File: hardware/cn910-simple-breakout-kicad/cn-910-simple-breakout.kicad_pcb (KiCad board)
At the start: 2 copper layers, 35 x 35 mm, 8 parts, among them J1 CN910_FPC_CON, J2 J_PB_RF, J3 J_REC_RF

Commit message: Enhanced CN910 breakout KiCad project with updated design rules, added new components, and refined PCB layout. Introduced a new simple breakout PCB with detailed Gerber files for manufacturing. Updated project metadata and library references for improved organization.
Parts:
- added R1: 470, Resistor_SMD:R_0603_1608Metric, F.Cu at (167.8, 93.3)
- added R2: 470, Resistor_SMD:R_0603_1608Metric, F.Cu at (167.8, 103.1)
- added TP2: TP_PB_RF, TestPoint:TestPoint_Pad_1.5x1.5mm, F.Cu at (168.4, 90.2)
- added TP3: TP_REC_RF, TestPoint:TestPoint_Pad_1.5x1.5mm, F.Cu at (172.7, 102.5)
- added TP4: TP_LANC_SIG, TestPoint:TestPoint_Loop_D2.50mm_Drill1.0mm, F.Cu at (151.1, 82.9)
- added TP5: TP_XCPC_IN, TestPoint:TestPoint_Loop_D2.50mm_Drill1.0mm, F.Cu at (155.2, 87.5)
- added TP6: TP_GND, TestPoint:TestPoint_Loop_D2.50mm_Drill1.0mm, F.Cu at (171.3, 96.4)
- moved TP1 9.24 mm to (160.5, 82.1)
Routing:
- net /LANC_SIG: track 0.00 -> 9.97 mm
- net /XCPC_IN: track 0.00 -> 9.58 mm
- net /REC_RF: track 19.9 -> 25.0 mm
- net /PB_RF: track 14.6 -> 19.4 mm
- net Net-(R2-Pad2): track 0.00 -> 4.47 mm
- net GND: vias 65 -> 69

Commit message: Refactored CN910 breakout KiCad project files, updating footprint and symbol references to "GDH" naming convention. Adjusted PCB thickness and dielectric properties for improved design accuracy. Added new adhesive layers and updated project metadata with a new variant description. Removed obsolete libraries and 3D models to streamline the project.
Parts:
- J1: footprint CN910:CON_527461671_MOL -> GDH Connectors:CON_527461671_MOL
- J2, J3: footprint CN910:GRADCONN_RFPC-SMA28-F -> GDH Connectors:GRADCONN_RFPC-SMA28-F
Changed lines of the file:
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@@
 		(embedded_fonts no)
 	)
-	(footprint "CN910:GRADCONN_RFPC-SMA28-F"
+	(footprint "GDH Connectors:GRADCONN_RFPC-SMA28-F"
 		(layer "F.Cu")
 		(at 162 103.7)
@@
 		)
 	)
-	(footprint "CN910:CON_527461671_MOL"
+	(footprint "GDH Connectors:CON_527461671_MOL"
 		(layer "F.Cu")
 		(at 145.05 95.15 -90)
@@
 		(embedded_fonts no)
 	)
-	(footprint "CN910:GRADCONN_RFPC-SMA28-F"
+	(footprint "GDH Connectors:GRADCONN_RFPC-SMA28-F"
 		(layer "F.Cu")
 		(at 162 93.899639)

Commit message: Updated CN910 breakout KiCad project files with dynamic project metadata, including title, company, version, and license. Refined design rules and component properties for improved clarity and organization. Adjusted pin functions and descriptions for connectors, and removed obsolete library references. Enhanced layout with new wire connections and updated schematic components.
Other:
- board text added: "⏚"

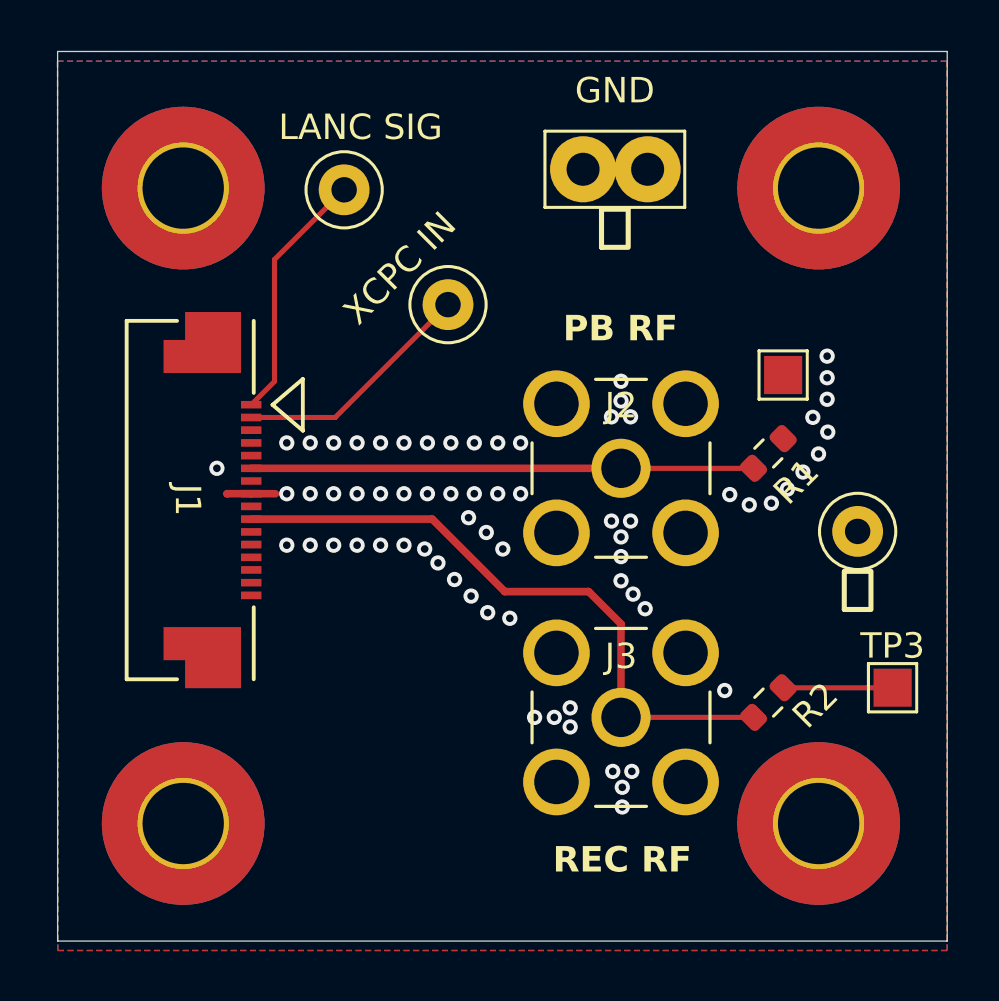
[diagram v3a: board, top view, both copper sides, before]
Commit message: Updated CN910 breakout KiCad project files to reflect JLCPCB manufacturing specifications, including revised design rules for track width, via dimensions, and hole clearances. Adjusted component properties and footprints for test points, ensuring accurate descriptions and tags. Enhanced project metadata with dynamic title and versioning, while streamlining schematic connections and layout for improved clarity.
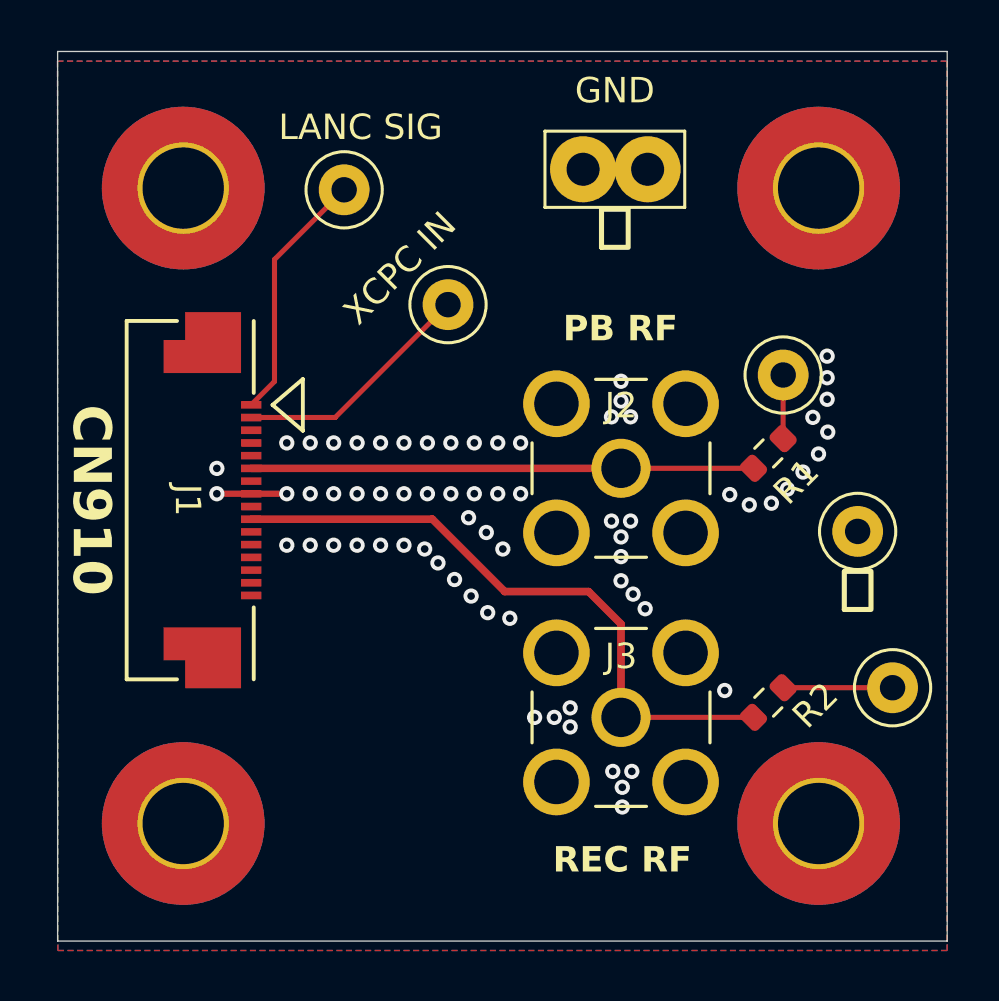
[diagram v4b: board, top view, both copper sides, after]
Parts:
- TP2, TP3: footprint TestPoint:TestPoint_Pad_1.5x1.5mm -> TestPoint:TestPoint_Loop_D2.50mm_Drill1.0mm
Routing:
- net Net-(R1-Pad2): track 0.00 -> 2.50 mm
- net GND: track 1.90 -> 2.75 mm, vias 69 -> 70
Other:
- board text added: "CN910"
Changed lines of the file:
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@@
 		(capping no)
 		(filling no)
+		(zone_defaults)
 		(grid_origin 196.325 112.375)
 		(pcbplotparams
@@
 	(property "proj-company" "GDH Technologies LLC")
 	(property "proj-license" "")
-	(property "proj-title" "CN910 Breakout")
+	(property "proj-title" "")
 	(property "proj-version" "1.0")
 	(footprint "Resistor_SMD:R_0603_1608Metric"
@@
 		(embedded_fonts no)
 	)
-	(footprint "TestPoint:TestPoint_Pad_1.5x1.5mm"
+	(footprint "TestPoint:TestPoint_Loop_D2.50mm_Drill1.0mm"
 		(layer "F.Cu")
 		(at 172.683727 102.533274)
-		(descr "SMD rectangular pad as test Point, square 1.5mm side length")
-		(tags "test point SMD pad rectangle square")
+		(descr "wire loop as test point, loop diameter 2.5mm, hole diameter 1.0mm")
+		(tags "test point wire loop bead")
 		(property "Reference" "TP3"
-			(at 0 -1.648 0)
+			(at -1.882368 -1.748945 45)
 			(layer "F.SilkS")
+			(hide yes)
 			(effects
 				(font
@@
 		)
 		(property "Value" "TP_REC_RF"
-			(at 0 1.75 0)
+			(at 0 -2.8 0)
 			(layer "F.Fab")
 			(effects
@@
 			)
 		)
+		(attr through_hole)
 		(duplicate_pad_numbers_are_jumpers no)
-		(fp_line
-			(start -0.95 -0.95)
-			(end 0.95 -0.95)
+		(fp_circle
+			(center 0 0)
+			(end 1.5 0)
 			(stroke
 				(width 0.12)
 				(type solid)
 			)
+			(fill no)
 			(layer "F.SilkS")
 		)
-		(fp_line
-			(start -0.95 0.95)
-			(end -0.95 -0.95)
+		(fp_circle
+			(center 0 0)
+			(end 1.8 0)
 			(stroke
-				(width 0.12)
+				(width 0.05)
 				(type solid)
 			)
-			(layer "F.SilkS")
+			(fill no)
+			(layer "F.CrtYd")
 		)
 		(fp_line
-			(start 0.95 -0.95)
-			(end 0.95 0.95)
+			(start -1.3 -0.2)
+			(end -1.3 0.2)
 			(stroke
 				(width 0.12)
 				(type solid)
 			)
-			(layer "F.SilkS")
+			(layer "F.Fab")
 		)
 		(fp_line
-			(start 0.95 0.95)
-			(end -0.95 0.95)
+			(start -1.3 0.2)
+			(end 1.3 0.2)
 			(stroke
 				(width 0.12)
 				(type solid)
 			)
-			(layer "F.SilkS")
-		)
-		(fp_line
-			(start -1.25 -1.25)
-			(end -1.25 1.25)
-			(stroke
-				(width 0.05)
-				(type solid)
-			)
-			(layer "F.CrtYd")
-		)
-		(fp_line
-			(start -1.25 -1.25)
-			(end 1.25 -1.25)
-			(stroke
-				(width 0.05)
-				(type solid)
-			)
-			(layer "F.CrtYd")
+			(layer "F.Fab")
 		)
 		(fp_line
-			(start 1.25 1.25)
-			(end -1.25 1.25)
+			(start 1.3 -0.2)
+			(end -1.3 -0.2)
 			(stroke
-				(width 0.05)
+				(width 0.12)
 				(type solid)
 			)
-			(layer "F.CrtYd")
+			(layer "F.Fab")
 		)
 		(fp_line
-			(start 1.25 1.25)
-			(end 1.25 -1.25)
+			(start 1.3 0.2)
+			(end 1.3 -0.2)
 			(stroke
-				(width 0.05)
+				(width 0.12)
 				(type solid)
 			)
-			(layer "F.CrtYd")
+			(layer "F.Fab")
 		)
 		(fp_text user "${REFERENCE}"
-			(at 0 -1.65 0)
+			(at 0.7 2.5 0)
 			(layer "F.Fab")
 			(effects
@@
 			)
 		)
-		(pad "1" smd rect
+		(pad "1" thru_hole circle
 			(at 0 0)
-			(size 1.5 1.5)
-			(layers "F.Cu" "F.Mask")
+			(size 2 2)
+			(drill 1)
+			(layers "*.Cu" "*.Mask")
+			(remove_unused_layers no)
 			(net "Net-(R2-Pad2)")
 			(pinfunction "1_1")
@@
 		)
 		(embedded_fonts no)
+		(model "${KICAD10_3DMODEL_DIR}/TestPoint.3dshapes/TestPoint_Loop_D2.50mm_Drill1.0mm.step"
+			(offset
+				(xyz 0 0 0)
+			)
+			(scale
+				(xyz 1 1 1)
+			)
+			(rotate
+				(xyz 0 0 0)
+			)
+		)
 	)
 	(footprint "GDH Connectors:GRADCONN_RFPC-SMA28-F"
@@
 	(footprint "GDH Connectors:CON_527461671_MOL"
 		(layer "F.Cu")
-		(at 145.05 95.15 -90)
+		(at 145.05 95.153131 -90)
 		(tags "527461671 ")
 		(property "Reference" "J1"
@@
 		)
 	)
-	(footprint "TestPoint:TestPoint_Pad_1.5x1.5mm"
+	(footprint "TestPoint:TestPoint_Loop_D2.50mm_Drill1.0mm"
 		(layer "F.Cu")
 		(at 168.379397 90.229338)
-		(descr "SMD rectangular pad as test Point, square 1.5mm side length")
-		(tags "test point SMD pad rectangle square")
+		(descr "wire loop as test point, loop diameter 2.5mm, hole diameter 1.0mm")
+		(tags "test point wire loop bead")
 		(property "Reference" "TP2"
-			(at 0 -1.648 0)
+			(at 0.7 2.5 0)
 			(layer "F.SilkS")
 			(hide yes)
@@
 		)
 		(property "Value" "TP_PB_RF"
-			(at 0 1.75 0)
+			(at 0 -2.8 0)
 			(layer "F.Fab")
-			(hide yes)
 			(effects
 				(font
@@
 			)
 		)
+		(attr through_hole)
 		(duplicate_pad_numbers_are_jumpers no)
-		(fp_line
-			(start -0.95 -0.95)
-			(end 0.95 -0.95)
+		(fp_circle
+			(center 0 0)
+			(end 1.5 0)
 			(stroke
 				(width 0.12)
 				(type solid)
 			)
+			(fill no)
 			(layer "F.SilkS")
 		)
-		(fp_line
-			(start -0.95 0.95)
-			(end -0.95 -0.95)
+		(fp_circle
+			(center 0 0)
+			(end 1.8 0)
 			(stroke
-				(width 0.12)
+				(width 0.05)
 				(type solid)
 			)
-			(layer "F.SilkS")
+			(fill no)
+			(layer "F.CrtYd")
 		)
 		(fp_line
-			(start 0.95 -0.95)
-			(end 0.95 0.95)
+			(start -1.3 -0.2)
+			(end -1.3 0.2)
 			(stroke
 				(width 0.12)
 				(type solid)
 			)
-			(layer "F.SilkS")
+			(layer "F.Fab")
 		)
 		(fp_line
-			(start 0.95 0.95)
-			(end -0.95 0.95)
+			(start -1.3 0.2)
+			(end 1.3 0.2)
 			(stroke
 				(width 0.12)
 				(type solid)
 			)
-			(layer "F.SilkS")
-		)
-		(fp_line
-			(start -1.25 -1.25)
-			(end -1.25 1.25)
-			(stroke
-				(width 0.05)
-				(type solid)
-			)
-			(layer "F.CrtYd")
-		)
-		(fp_line
-			(start -1.25 -1.25)
-			(end 1.25 -1.25)
-			(stroke
-				(width 0.05)
-				(type solid)
-			)
-			(layer "F.CrtYd")
+			(layer "F.Fab")
 		)
 		(fp_line
-			(start 1.25 1.25)
-			(end -1.25 1.25)
+			(start 1.3 -0.2)
+			(end -1.3 -0.2)
 			(stroke
-				(width 0.05)
+				(width 0.12)
 				(type solid)
 			)
-			(layer "F.CrtYd")
+			(layer "F.Fab")
 		)
 		(fp_line
-			(start 1.25 1.25)
-			(end 1.25 -1.25)
+			(start 1.3 0.2)
+			(end 1.3 -0.2)
 			(stroke
-				(width 0.05)
+				(width 0.12)
 				(type solid)
 			)
-			(layer "F.CrtYd")
+			(layer "F.Fab")
 		)
 		(fp_text user "${REFERENCE}"
-			(at 0 -1.65 0)
+			(at 0.7 2.5 0)
 			(layer "F.Fab")
 			(effects
@@
 			)
 		)
-		(pad "1" smd rect
+		(pad "1" thru_hole circle
 			(at 0 0)
-			(size 1.5 1.5)
-			(layers "F.Cu" "F.Mask")
+			(size 2 2)
+			(drill 1)
+			(layers "*.Cu" "*.Mask")
+			(remove_unused_layers no)
 			(net "Net-(R1-Pad2)")
 			(pinfunction "1_1")
@@
 		)
 		(embedded_fonts no)
+		(model "${KICAD10_3DMODEL_DIR}/TestPoint.3dshapes/TestPoint_Loop_D2.50mm_Drill1.0mm.step"
+			(offset
+				(xyz 0 0 0)
+			)
+			(scale
+				(xyz 1 1 1)
+			)
+			(rotate
+				(xyz 0 0 0)
+			)
+		)
 	)
 	(footprint "MountingHole:MountingHole_3.2mm_M3_Pad_TopBottom"
@@
 		)
 	)
+	(gr_text "CN910"
+		(at 141.164423 95.153131 270)
+		(layer "F.SilkS")
+		(effects
+			(font
+				(size 1.5 1.5)
+				(thickness 0.3)
+				(bold yes)
+			)
+		)
+	)
 	(dimension
 		(type orthogonal)
@@
 	)
 	(segment
-		(start 147.45 94.900008)
-		(end 148.4 94.900008)
-		(width 0.3)
+		(start 147.450008 94.9)
+		(end 147.45 94.900008)
+		(width 0.25)
 		(layer "F.Cu")
 		(net "GND")
 	)
 	(segment
-		(start 147.45 94.900008)
-		(end 146.500008 94.900008)
-		(width 0.3)
+		(start 148.85 94.9)
+		(end 147.450008 94.9)
+		(width 0.25)
 		(layer "F.Cu")
 		(net "GND")
 	)
 	(segment
-		(start 146.500008 94.900008)
-		(end 146.5 94.9)
-		(width 0.3)
+		(start 146.098578 94.900008)
+		(end 147.45 94.900008)
+		(width 0.25)
 		(layer "F.Cu")
 		(net "GND")
@@
 	)
 	(via
+		(at 146.098578 93.903139)
+		(size 0.6)
+		(drill 0.3)
+		(layers "F.Cu" "B.Cu")
+		(free yes)
+		(net "GND")
+	)
+	(via
 		(at 156.227778 92.900008)
 		(size 0.6)
@@
 	)
 	(via
-		(at 146.1 93.9)
+		(at 146.098578 94.900008)
 		(size 0.6)
 		(drill 0.3)
@@
 		(net "/PB_RF")
 	)
+	(segment
+		(start 168.379397 90.229338)
+		(end 168.379397 92.732913)
+		(width 0.2)
+		(layer "F.Cu")
+		(net "Net-(R1-Pad2)")
+	)
 	(zone
